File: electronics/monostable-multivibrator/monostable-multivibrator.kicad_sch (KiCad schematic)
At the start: 21 parts, among them J1 VCC_IN, J2 GND_IN, J3 LOAD_VIN, J4 LOAD_COM, Q1 2N3904, SW1 SW_TRIG, SW2 SW_BYPASS, U1 NE555P, U2 LM7805_TO220

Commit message: nice silkscreen updates
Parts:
- removed J1: VCC_IN, Connector_PinHeader_2.00mm:PinHeader_1x01_P2.00mm_Vertical, symbol Connector:Conn_01x01_Socket
- removed J2: GND_IN, Connector_PinHeader_2.00mm:PinHeader_1x01_P2.00mm_Vertical, symbol Connector:Conn_01x01_Socket
- removed J3: LOAD_VIN, Connector_PinHeader_2.00mm:PinHeader_1x01_P2.00mm_Vertical, symbol Connector:Conn_01x01_Socket
- removed J4: LOAD_COM, Connector_PinHeader_2.00mm:PinHeader_1x01_P2.00mm_Vertical, symbol Connector:Conn_01x01_Socket
- added J1: PWR, Connector_PinSocket_2.54mm:PinSocket_1x02_P2.54mm_Vertical, symbol Connector:Conn_01x02_Socket
- added J2: LOAD, Connector_PinSocket_2.54mm:PinSocket_1x02_P2.54mm_Vertical, symbol Connector:Conn_01x02_Socket
- C2, C3, C4: footprint Capacitor_THT:C_Disc_D3.0mm_W1.6mm_P2.50mm -> Capacitor_THT:C_Disc_D4.3mm_W1.9mm_P5.00mm
- SW1: value SW_TRIG -> CO NO NC
- SW2: value SW_BYPASS -> + -
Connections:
- net GND: now also J1.2 (Pin_2)
- net VCC: now also J1.1 (Pin_1), J2.1 (Pin_1)
- net LOAD_COM: now reaches D1.2 (A), Q1.3 (C)
- net LOAD_COM: now also J2.2 (Pin_2)
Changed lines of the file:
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@@
   (junction (at 142.24 123.19) (diameter 0) (color 0 0 0 0)
   )
+  (junction (at 219.71 115.57) (diameter 0) (color 0 0 0 0)
+  )
   (junction (at 193.04 129.54) (diameter 0) (color 0 0 0 0)
   )
+  (junction (at 219.71 107.95) (diameter 0) (color 0 0 0 0)
+  )
   (junction (at 82.55 57.15) (diameter 0) (color 0 0 0 0)
   )
-  (junction (at 219.71 115.57) (diameter 0) (color 0 0 0 0)
+  (junction (at 93.98 24.13) (diameter 0) (color 0 0 0 0)
+  )
+  (junction (at 93.98 29.21) (diameter 0) (color 0 0 0 0)
+  )
+  (junction (at 223.52 115.57) (diameter 0) (color 0 0 0 0)
   )
   (junction (at 91.44 57.15) (diameter 0) (color 0 0 0 0)
   )
-  (junction (at 93.98 24.13) (diameter 0) (color 0 0 0 0)
-  )
-  (junction (at 93.98 29.21) (diameter 0) (color 0 0 0 0)
-  )
   (junction (at 142.24 128.27) (diameter 0) (color 0 0 0 0)
   )
@@
   (junction (at 106.68 67.31) (diameter 0) (color 0 0 0 0)
   )
-  (junction (at 219.71 107.95) (diameter 0) (color 0 0 0 0)
-  )
   (wire (pts (xy 193.04 107.95) (xy 182.88 107.95))
     (stroke (width 0) (type default))
@@
     (stroke (width 0) (type default))
   )
+  (wire (pts (xy 93.98 26.67) (xy 93.98 29.21))
+    (stroke (width 0) (type default))
+  )
   (wire (pts (xy 110.49 100.33) (xy 110.49 113.03))
     (stroke (width 0) (type default))
   )
+  (wire (pts (xy 223.52 107.95) (xy 219.71 107.95))
+    (stroke (width 0) (type default))
+  )
   (wire (pts (xy 82.55 78.74) (xy 99.06 78.74))
     (stroke (width 0) (type default))
@@
     (stroke (width 0) (type default))
   )
+  (wire (pts (xy 223.52 115.57) (xy 219.71 115.57))
+    (stroke (width 0) (type default))
+  )
   (wire (pts (xy 123.19 123.19) (xy 142.24 123.19))
     (stroke (width 0) (type default))
@@
     (stroke (width 0) (type default))
   )
+  (wire (pts (xy 223.52 115.57) (xy 223.52 118.11))
+    (stroke (width 0) (type default))
+  )
   (wire (pts (xy 85.09 24.13) (xy 93.98 24.13))
     (stroke (width 0) (type default))
@@
     (stroke (width 0) (type default))
   )
+  (wire (pts (xy 223.52 111.76) (xy 223.52 115.57))
+    (stroke (width 0) (type default))
+  )
+  (wire (pts (xy 223.52 109.22) (xy 223.52 107.95))
+    (stroke (width 0) (type default))
+  )
   (wire (pts (xy 123.19 128.27) (xy 142.24 128.27))
     (stroke (width 0) (type default))
@@
     (effects (font (size 1.27 1.27)) (justify left bottom))
   )
+  (label "LOAD_VIN" (at 223.52 107.95 0) (fields_autoplaced)
+    (effects (font (size 1.27 1.27)) (justify left bottom))
+  )
   (label "555_VIN" (at 182.88 107.95 0) (fields_autoplaced)
+    (effects (font (size 1.27 1.27)) (justify left bottom))
+  )
+  (label "LOAD_COM" (at 223.52 118.11 0) (fields_autoplaced)
     (effects (font (size 1.27 1.27)) (justify left bottom))
   )
@@
       (effects (font (size 1.27 1.27)))
     )
-    (property "Footprint" "Capacitor_THT:C_Disc_D3.0mm_W1.6mm_P2.50mm" (at 74.93 122.2248 0)
+    (property "Footprint" "Capacitor_THT:C_Disc_D4.3mm_W1.9mm_P5.00mm" (at 74.93 122.2248 0)
       (effects (font (size 1.27 1.27)) hide)
     )
@@
         (path "/db104dae-9550-49a8-a6a2-ffb5f77a0160"
           (reference "C2") (unit 1)
-        )
-      )
-    )
-  )
-  (symbol (lib_id "Connector:Conn_01x01_Socket") (at 224.79 107.95 0) (unit 1)
-    (in_bom yes) (on_board yes) (dnp no)
-    (property "Reference" "J3" (at 226.06 106.68 0)
-      (effects (font (size 1.27 1.27)) (justify left))
-    )
-    (property "Value" "LOAD_VIN" (at 226.06 109.22 0)
-      (effects (font (size 1.27 1.27)) (justify left))
-    )
-    (property "Footprint" "Connector_PinHeader_2.00mm:PinHeader_1x01_P2.00mm_Vertical" (at 224.79 107.95 0)
-      (effects (font (size 1.27 1.27)) hide)
-    )
-    (property "Datasheet" "~" (at 224.79 107.95 0)
-      (effects (font (size 1.27 1.27)) hide)
-    )
-    (pin "1")
-    (instances
-      (project "monostable-multivibrator"
-        (path "/db104dae-9550-49a8-a6a2-ffb5f77a0160"
-          (reference "J3") (unit 1)
         )
       )
@@
       (effects (font (size 1.27 1.27)) (justify right))
     )
-    (property "Value" "SW_BYPASS" (at 194.31 114.3 90)
+    (property "Value" "+ -" (at 194.31 114.3 90)
       (effects (font (size 1.27 1.27)) (justify right))
     )
@@
         (path "/db104dae-9550-49a8-a6a2-ffb5f77a0160"
           (reference "SW2") (unit 1)
-        )
-      )
-    )
-  )
-  (symbol (lib_id "Connector:Conn_01x01_Socket") (at 224.79 115.57 0) (unit 1)
-    (in_bom yes) (on_board yes) (dnp no)
-    (property "Reference" "J4" (at 226.06 114.3 0)
-      (effects (font (size 1.27 1.27)) (justify left))
-    )
-    (property "Value" "LOAD_COM" (at 226.06 116.84 0)
-      (effects (font (size 1.27 1.27)) (justify left))
-    )
-    (property "Footprint" "Connector_PinHeader_2.00mm:PinHeader_1x01_P2.00mm_Vertical" (at 224.79 115.57 0)
-      (effects (font (size 1.27 1.27)) hide)
-    )
-    (property "Datasheet" "~" (at 224.79 115.57 0)
-      (effects (font (size 1.27 1.27)) hide)
-    )
-    (pin "1")
-    (instances
-      (project "monostable-multivibrator"
-        (path "/db104dae-9550-49a8-a6a2-ffb5f77a0160"
-          (reference "J4") (unit 1)
         )
       )
@@
     )
   )
+  (symbol (lib_id "Connector:Conn_01x02_Socket") (at 228.6 109.22 0) (unit 1)
+    (in_bom yes) (on_board yes) (dnp no) (fields_autoplaced)
+    (property "Reference" "J2" (at 229.87 109.22 0)
+      (effects (font (size 1.27 1.27)) (justify left))
+    )
+    (property "Value" "LOAD" (at 229.87 111.76 0)
+      (effects (font (size 1.27 1.27)) (justify left))
+    )
+    (property "Footprint" "Connector_PinSocket_2.54mm:PinSocket_1x02_P2.54mm_Vertical" (at 228.6 109.22 0)
+      (effects (font (size 1.27 1.27)) hide)
+    )
+    (property "Datasheet" "~" (at 228.6 109.22 0)
+      (effects (font (size 1.27 1.27)) hide)
+    )
+    (pin "1")
+    (pin "2")
+    (instances
+      (project "monostable-multivibrator"
+        (path "/db104dae-9550-49a8-a6a2-ffb5f77a0160"
+          (reference "J2") (unit 1)
+        )
+      )
+    )
+  )
   (symbol (lib_id "power:VCC") (at 82.55 57.15 0) (unit 1)
     (in_bom yes) (on_board yes) (dnp no) (fields_autoplaced)
@@
       (effects (font (size 1.27 1.27)) (justify left))
     )
-    (property "Footprint" "Capacitor_THT:C_Disc_D3.0mm_W1.6mm_P2.50mm" (at 107.6452 76.2 0)
+    (property "Footprint" "Capacitor_THT:C_Disc_D4.3mm_W1.9mm_P5.00mm" (at 107.6452 76.2 0)
       (effects (font (size 1.27 1.27)) hide)
     )
@@
     )
   )
+  (symbol (lib_id "Connector:Conn_01x02_Socket") (at 99.06 24.13 0) (unit 1)
+    (in_bom yes) (on_board yes) (dnp no) (fields_autoplaced)
+    (property "Reference" "J1" (at 100.33 24.13 0)
+      (effects (font (size 1.27 1.27)) (justify left))
+    )
+    (property "Value" "PWR" (at 100.33 26.67 0)
+      (effects (font (size 1.27 1.27)) (justify left))
+    )
+    (property "Footprint" "Connector_PinSocket_2.54mm:PinSocket_1x02_P2.54mm_Vertical" (at 99.06 24.13 0)
+      (effects (font (size 1.27 1.27)) hide)
+    )
+    (property "Datasheet" "~" (at 99.06 24.13 0)
+      (effects (font (size 1.27 1.27)) hide)
+    )
+    (pin "1")
+    (pin "2")
+    (instances
+      (project "monostable-multivibrator"
+        (path "/db104dae-9550-49a8-a6a2-ffb5f77a0160"
+          (reference "J1") (unit 1)
+        )
+      )
+    )
+  )
   (symbol (lib_id "power:GND") (at 142.24 142.24 0) (unit 1)
     (in_bom yes) (on_board yes) (dnp no) (fields_autoplaced)
@@
         (path "/db104dae-9550-49a8-a6a2-ffb5f77a0160"
           (reference "C1") (unit 1)
-        )
-      )
-    )
-  )
-  (symbol (lib_id "Connector:Conn_01x01_Socket") (at 99.06 24.13 0) (unit 1)
-    (in_bom yes) (on_board yes) (dnp no) (fields_autoplaced)
-    (property "Reference" "J1" (at 100.33 22.86 0)
-      (effects (font (size 1.27 1.27)) (justify left))
-    )
-    (property "Value" "VCC_IN" (at 100.33 25.4 0)
-      (effects (font (size 1.27 1.27)) (justify left))
-    )
-    (property "Footprint" "Connector_PinHeader_2.00mm:PinHeader_1x01_P2.00mm_Vertical" (at 99.06 24.13 0)
-      (effects (font (size 1.27 1.27)) hide)
-    )
-    (property "Datasheet" "~" (at 99.06 24.13 0)
-      (effects (font (size 1.27 1.27)) hide)
-    )
-    (pin "1")
-    (instances
-      (project "monostable-multivibrator"
-        (path "/db104dae-9550-49a8-a6a2-ffb5f77a0160"
-          (reference "J1") (unit 1)
         )
       )
@@
       (effects (font (size 1.27 1.27)) (justify right))
     )
-    (property "Value" "SW_TRIG" (at 86.36 114.3 90)
+    (property "Value" "CO NO NC" (at 86.36 114.3 90)
       (effects (font (size 1.27 1.27)) (justify right))
     )
@@
       (effects (font (size 1.27 1.27)) (justify left))
     )
-    (property "Footprint" "Capacitor_THT:C_Disc_D3.0mm_W1.6mm_P2.50mm" (at 83.5152 76.2 0)
+    (property "Footprint" "Capacitor_THT:C_Disc_D4.3mm_W1.9mm_P5.00mm" (at 83.5152 76.2 0)
       (effects (font (size 1.27 1.27)) hide)
     )
@@
         )
       )
-    )
-  )
-  (symbol (lib_id "Connector:Conn_01x01_Socket") (at 99.06 29.21 0) (unit 1)
-    (in_bom yes) (on_board yes) (dnp no) (fields_autoplaced)
-    (property "Reference" "J2" (at 100.33 27.94 0)
-      (effects (font (size 1.27 1.27)) (justify left))
-    )
-    (property "Value" "GND_IN" (at 100.33 30.48 0)
-      (effects (font (size 1.27 1.27)) (justify left))
-    )
-    (property "Footprint" "Connector_PinHeader_2.00mm:PinHeader_1x01_P2.00mm_Vertical" (at 99.06 29.21 0)
-      (effects (font (size 1.27 1.27)) hide)
-    )
-    (property "Datasheet" "~" (at 99.06 29.21 0)
-      (effects (font (size 1.27 1.27)) hide)
-    )
-    (pin "1")
-    (instances
-      (project "monostable-multivibrator"
-        (path "/db104dae-9550-49a8-a6a2-ffb5f77a0160"
-          (reference "J2") (unit 1)
-        )
-      )

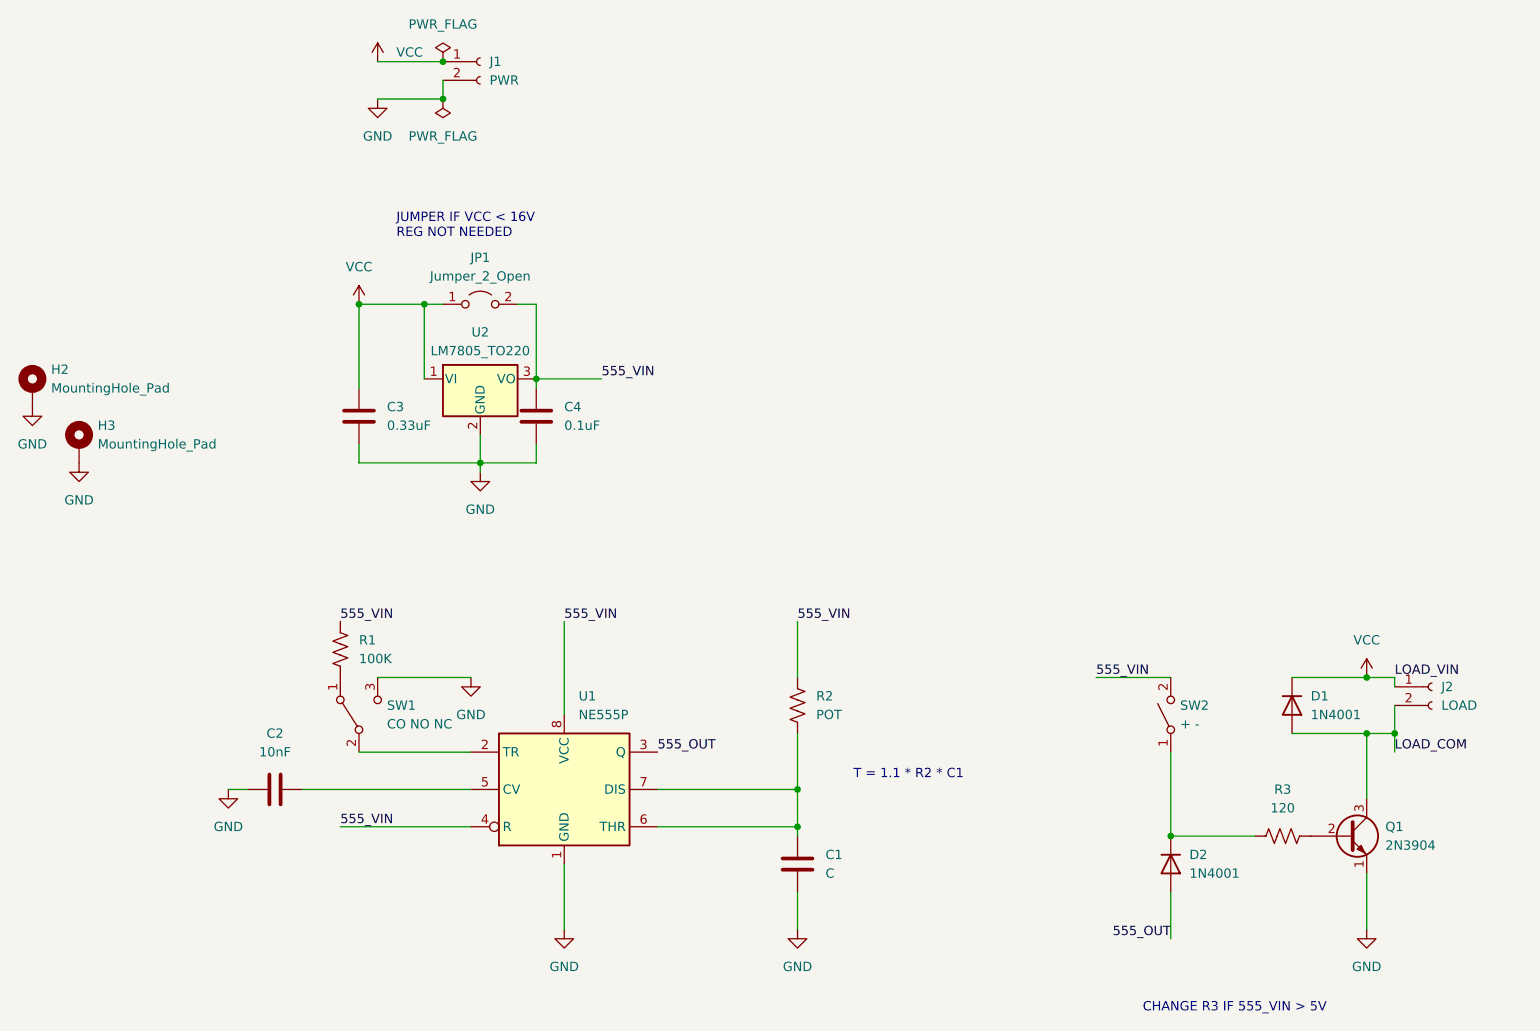
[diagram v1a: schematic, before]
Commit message: added cap to fix repeated triggers
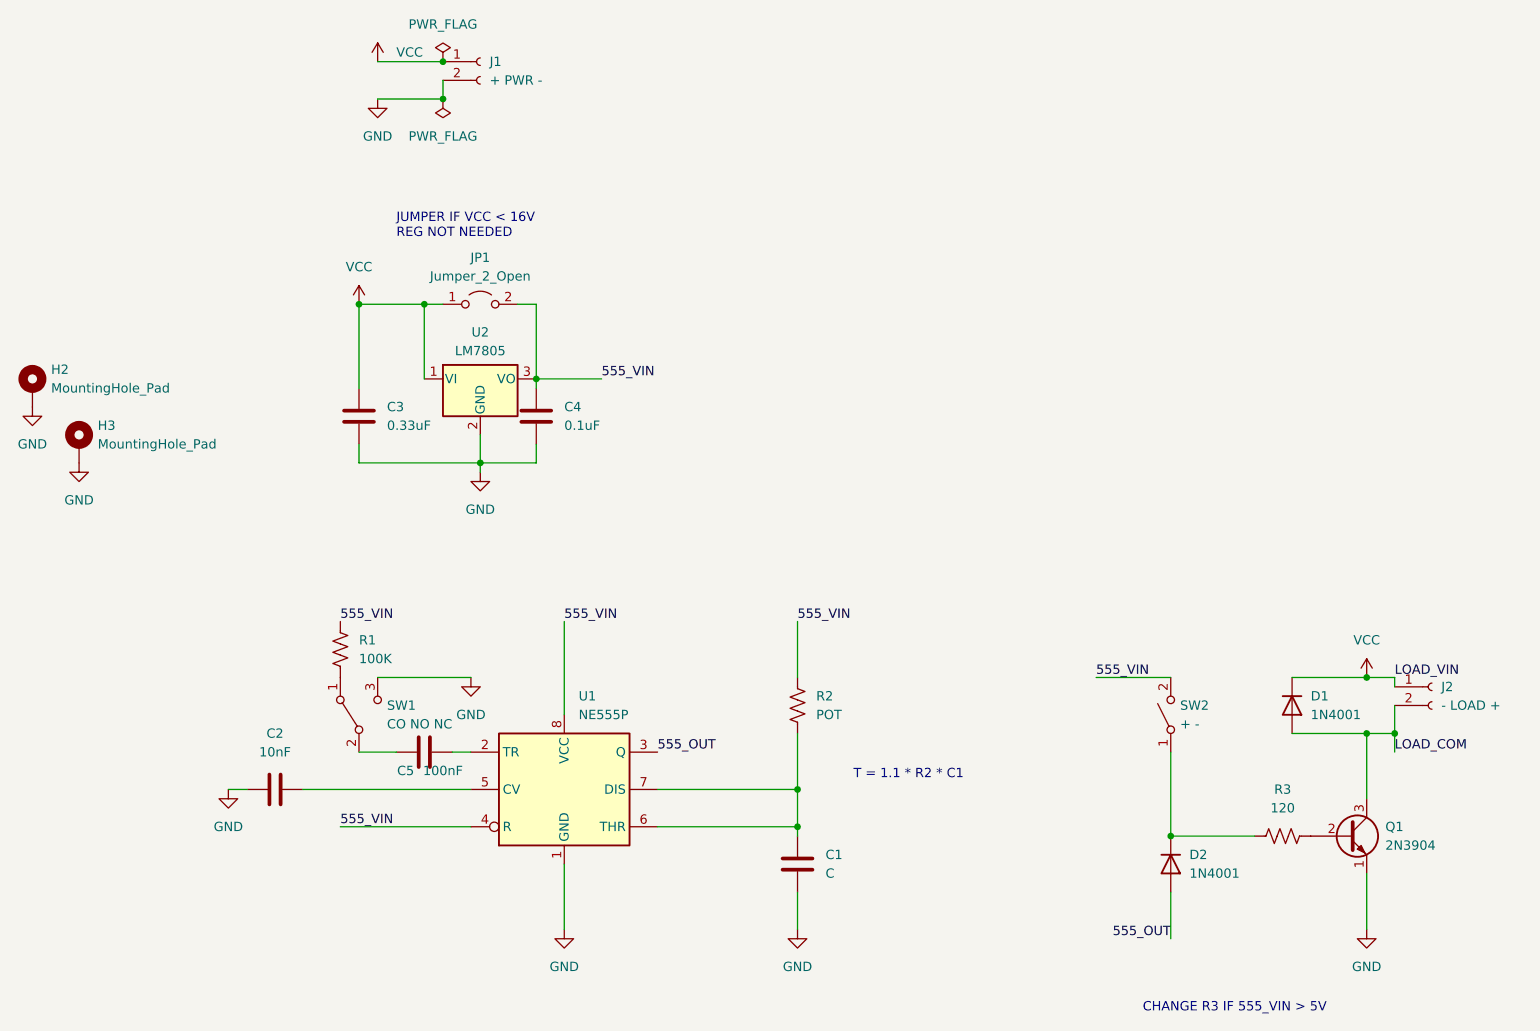
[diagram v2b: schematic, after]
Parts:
- added C5: 100nF, Capacitor_THT:C_Disc_D4.3mm_W1.9mm_P5.00mm, symbol Device:C
- J1: value PWR -> + PWR -
- J2: value LOAD -> - LOAD +
- U2: value LM7805_TO220 -> LM7805
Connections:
- net at U1.2 (TR): now also C5.1; no longer SW1.2 (B)
- new net: C5.2, SW1.2 (B)
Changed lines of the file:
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@@
-    (stroke (width 0) (type default))
-  )
-  (wire (pts (xy 82.55 118.11) (xy 97.79 118.11))
     (stroke (width 0) (type default))
   )
@@
     (stroke (width 0) (type default))
   )
+  (wire (pts (xy 82.55 118.11) (xy 87.63 118.11))
+    (stroke (width 0) (type default))
+  )
   (wire (pts (xy 82.55 57.15) (xy 91.44 57.15))
     (stroke (width 0) (type default))
@@
   )
   (wire (pts (xy 123.19 123.19) (xy 142.24 123.19))
+    (stroke (width 0) (type default))
+  )
+  (wire (pts (xy 95.25 118.11) (xy 97.79 118.11))
     (stroke (width 0) (type default))
   )
@@
         (path "/db104dae-9550-49a8-a6a2-ffb5f77a0160"
           (reference "JP1") (unit 1)
+        )
+      )
+    )
+  )
+  (symbol (lib_id "Device:C") (at 91.44 118.11 270) (unit 1)
+    (in_bom yes) (on_board yes) (dnp no)
+    (property "Reference" "C5" (at 88.9 120.65 90)
+      (effects (font (size 1.27 1.27)))
+    )
+    (property "Value" "100nF" (at 93.98 120.65 90)
+      (effects (font (size 1.27 1.27)))
+    )
+    (property "Footprint" "Capacitor_THT:C_Disc_D4.3mm_W1.9mm_P5.00mm" (at 87.63 119.0752 0)
+      (effects (font (size 1.27 1.27)) hide)
+    )
+    (property "Datasheet" "~" (at 91.44 118.11 0)
+      (effects (font (size 1.27 1.27)) hide)
+    )
+    (pin "1")
+    (pin "2")
+    (instances
+      (project "monostable-multivibrator"
+        (path "/db104dae-9550-49a8-a6a2-ffb5f77a0160"
+          (reference "C5") (unit 1)
         )
       )
@@
       (effects (font (size 1.27 1.27)) (justify left))
     )
-    (property "Value" "LOAD" (at 229.87 111.76 0)
+    (property "Value" "- LOAD +" (at 229.87 111.76 0)
       (effects (font (size 1.27 1.27)) (justify left))
     )
@@
       (effects (font (size 1.27 1.27)) (justify left))
     )
-    (property "Value" "PWR" (at 100.33 26.67 0)
+    (property "Value" "+ PWR -" (at 100.33 26.67 0)
       (effects (font (size 1.27 1.27)) (justify left))
     )
@@
       (effects (font (size 1.27 1.27)))
     )
-    (property "Value" "LM7805_TO220" (at 99.06 63.5 0)
-      (effects (font (size 1.27 1.27)))
-    )
+    (property "Value" "LM7805" (at 99.06 63.5 0)
+      (effects (font (size 1.27 1.27)))
+    )
